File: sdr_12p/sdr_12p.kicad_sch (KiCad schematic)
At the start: 8 parts, among them J1 Rx, J10 ADAU1467_GPIOS, J11 ADAU1467_AUX_ADCS, J4 6V, J6 Microcontroller, J7 USBi, J8 I2S2, J9 I2S1

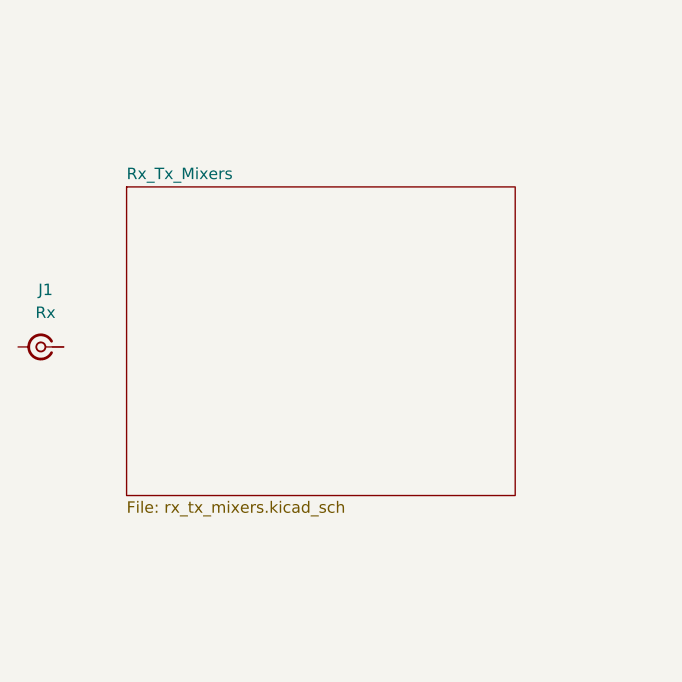
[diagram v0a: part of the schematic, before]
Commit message: fixed mixer page
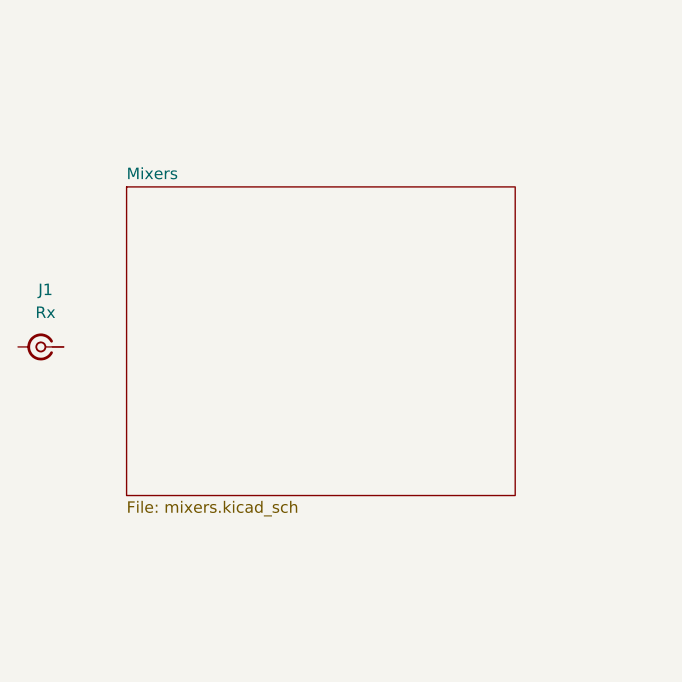
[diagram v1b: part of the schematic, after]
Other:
- sheet Rx_Tx_Mixers renamed Mixers
- sheet Mixers: file rx_tx_mixers.kicad_sch -> mixers.kicad_sch
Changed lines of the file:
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@@
 		)
 		(instances
-			(project "sdr_16p"
+			(project "sdr_12p"
 				(path "/fe42ca2f-2bb8-4d5a-9e84-807788ed632f"
 					(page "3")
@@
 		)
 		(instances
-			(project "sdr_16p"
+			(project "sdr_12p"
 				(path "/fe42ca2f-2bb8-4d5a-9e84-807788ed632f"
 					(page "10")
@@
 		)
 		(instances
-			(project "sdr_16p"
+			(project "sdr_12p"
 				(path "/fe42ca2f-2bb8-4d5a-9e84-807788ed632f"
 					(page "11")
@@
 		)
 		(instances
-			(project "sdr_16p"
+			(project "sdr_12p"
 				(path "/fe42ca2f-2bb8-4d5a-9e84-807788ed632f"
 					(page "7")
@@
 		)
 		(instances
-			(project "sdr_16p"
+			(project "sdr_12p"
 				(path "/fe42ca2f-2bb8-4d5a-9e84-807788ed632f"
 					(page "8")
@@
 		)
 		(instances
-			(project "sdr_16p"
+			(project "sdr_12p"
 				(path "/fe42ca2f-2bb8-4d5a-9e84-807788ed632f"
 					(page "2")
@@
 		)
 		(instances
-			(project "sdr_16p"
+			(project "sdr_12p"
 				(path "/fe42ca2f-2bb8-4d5a-9e84-807788ed632f"
 					(page "9")
@@
 			(color 0 0 0 0.0000)
 		)
-		(property "Sheetname" "Rx_Tx_Mixers"
+		(property "Sheetname" "Mixers"
 			(at 51.435 84.3784 0)
 			(effects
@@
 			)
 		)
-		(property "Sheetfile" "rx_tx_mixers.kicad_sch"
+		(property "Sheetfile" "mixers.kicad_sch"
 			(at 51.435 119.9646 0)
 			(effects
@@
 		)
 		(instances
-			(project "sdr_16p"
+			(project "sdr_12p"
 				(path "/fe42ca2f-2bb8-4d5a-9e84-807788ed632f"
 					(page "5")
@@
 		)
 		(instances
-			(project "sdr_16p"
+			(project "sdr_12p"
 				(path "/fe42ca2f-2bb8-4d5a-9e84-807788ed632f"
 					(page "12")
@@
 		)
 		(instances
-			(project "sdr_16p"
+			(project "sdr_12p"
 				(path "/fe42ca2f-2bb8-4d5a-9e84-807788ed632f"
 					(page "11")
@@
 		)
 		(instances
-			(project "sdr_16p"
+			(project "sdr_12p"
 				(path "/fe42ca2f-2bb8-4d5a-9e84-807788ed632f"
 					(page "4")

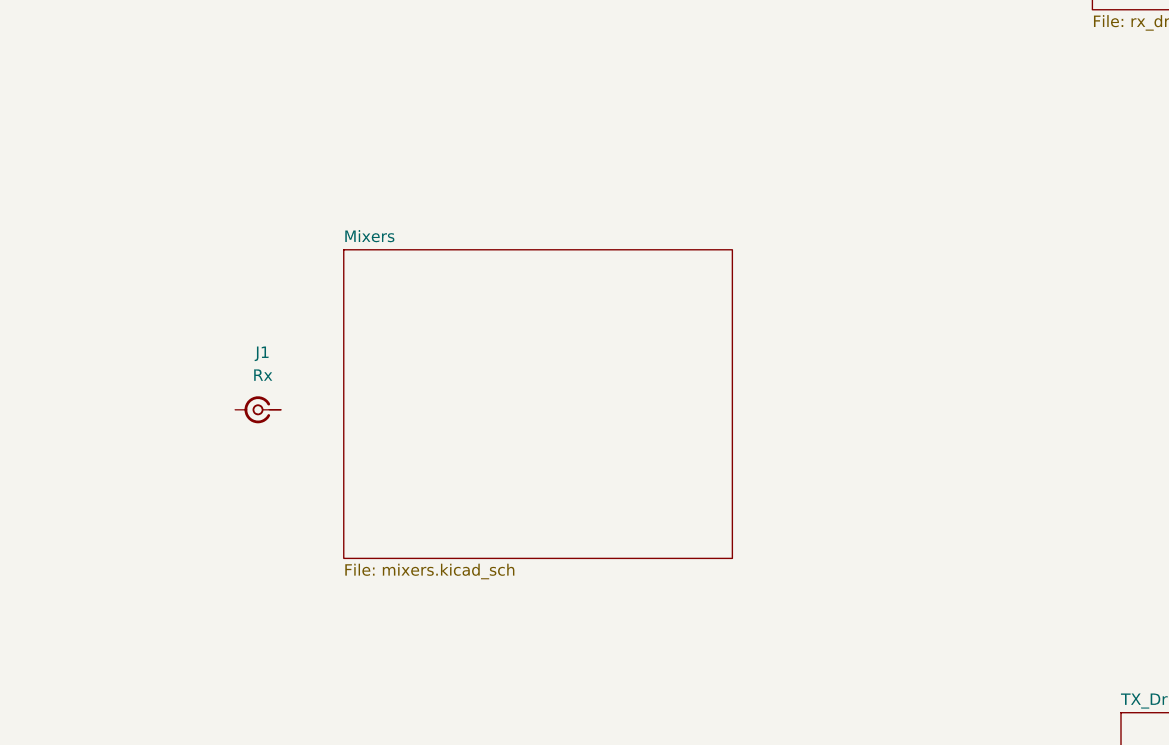
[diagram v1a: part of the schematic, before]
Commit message: fixed ldos for Clocks and DAP
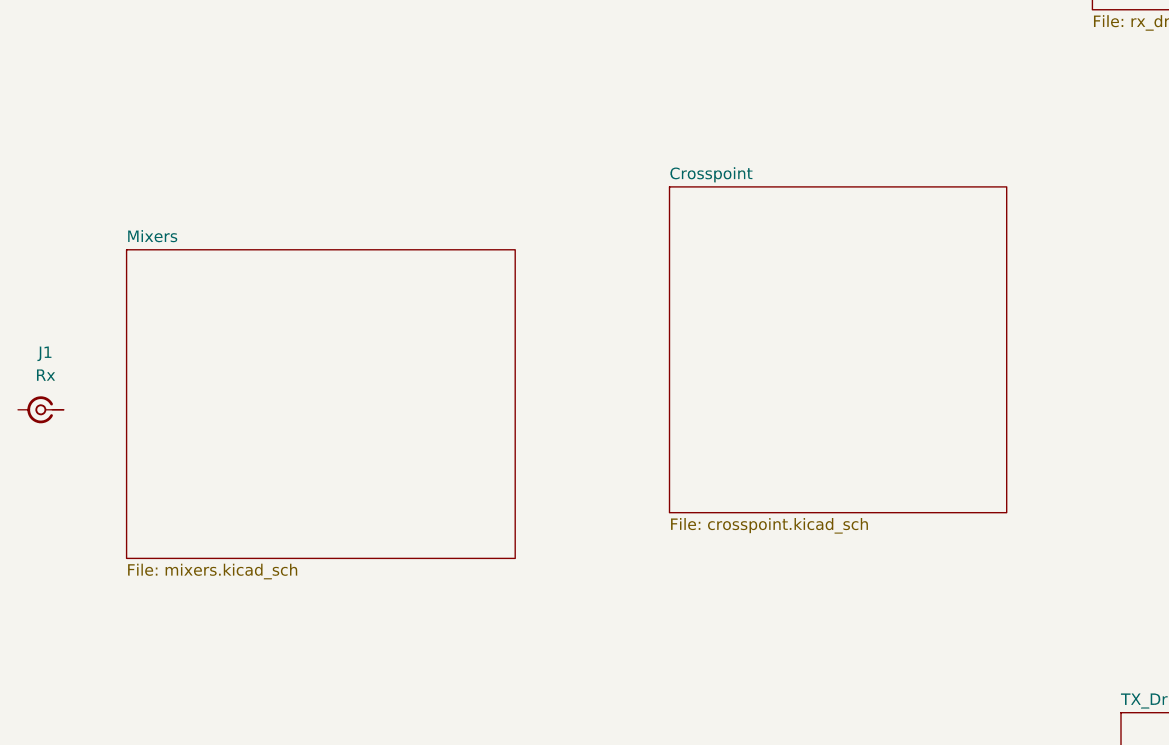
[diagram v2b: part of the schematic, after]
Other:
- added sheet Crosspoint (crosspoint.kicad_sch)
- moved on the sheet: J1
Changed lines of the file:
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@@
 	(symbol
 		(lib_id "Connector:Conn_Coaxial_Small")
-		(at 41.91 102.87 180)
+		(at 17.78 102.87 180)
 		(unit 1)
 		(exclude_from_sim no)
@@
 		(fields_autoplaced yes)
 		(property "Reference" "J1"
-			(at 42.4295 96.52 0)
+			(at 18.2995 96.52 0)
 			(effects
 				(font
@@
 		)
 		(property "Value" "Rx"
-			(at 42.4295 99.06 0)
+			(at 18.2995 99.06 0)
 			(effects
 				(font
@@
 		)
 		(property "Footprint" ""
-			(at 41.91 102.87 0)
+			(at 17.78 102.87 0)
 			(effects
 				(font
@@
 		)
 		(property "Datasheet" "~"
-			(at 41.91 102.87 0)
+			(at 17.78 102.87 0)
 			(effects
 				(font
@@
 		)
 		(property "Description" "small coaxial connector (BNC, SMA, SMB, SMC, Cinch/RCA, LEMO, ...)"
-			(at 41.91 102.87 0)
+			(at 17.78 102.87 0)
 			(effects
 				(font
@@
 	)
 	(sheet
-		(at 120.65 197.485)
-		(size 116.84 27.94)
+		(at 87.63 78.105)
+		(size 37.465 36.195)
 		(exclude_from_sim no)
 		(in_bom yes)
@@
 			(color 0 0 0 0.0000)
 		)
+		(property "Sheetname" "Crosspoint"
+			(at 87.63 77.3934 0)
+			(effects
+				(font
+					(size 1.27 1.27)
+				)
+				(justify left bottom)
+			)
+		)
+		(property "Sheetfile" "crosspoint.kicad_sch"
+			(at 87.63 114.8846 0)
+			(effects
+				(font
+					(size 1.27 1.27)
+				)
+				(justify left top)
+			)
+		)
+		(instances
+			(project "sdr_12p"
+				(path "/fe42ca2f-2bb8-4d5a-9e84-807788ed632f"
+					(page "13")
+				)
+			)
+		)
+	)
+	(sheet
+		(at 120.65 197.485)
+		(size 116.84 27.94)
+		(exclude_from_sim no)
+		(in_bom yes)
+		(on_board yes)
+		(dnp no)
+		(fields_autoplaced yes)
+		(stroke
+			(width 0.1524)
+			(type solid)
+		)
+		(fill
+			(color 0 0 0 0.0000)
+		)
 		(property "Sheetname" "Microcontroller"
 			(at 120.65 196.7734 0)
@@
 	)
 	(sheet
-		(at 51.435 85.09)
+		(at 27.305 85.09)
 		(size 43.18 34.29)
 		(exclude_from_sim no)
@@
 		)
 		(property "Sheetname" "Mixers"
-			(at 51.435 84.3784 0)
+			(at 27.305 84.3784 0)
 			(effects
 				(font
@@
 		)
 		(property "Sheetfile" "mixers.kicad_sch"
-			(at 51.435 119.9646 0)
-			(effects
-				(font
+			(at 27.305 119.9646 0)
+			(effects
+				(font
